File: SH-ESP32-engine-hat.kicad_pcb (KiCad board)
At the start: 2 copper layers, 34 x 58 mm, 66 parts, among them J301 I2C_top, J302 I2C_bottom, J303 GPIO subset, J304 Opto_bottom, J305 1-Wire_top, J306 1-Wire_bottom, J307 Opto_top, J401 Conn_01x02, J402 Conn_01x02, J501 Conn_01x02, J601 Alarm input, Q401 S9015, Q402 S9015, U401 LMV324, U402 RCLAMP0524P-N, U403 RCLAMP0524P-N, U601 ELQ3H7

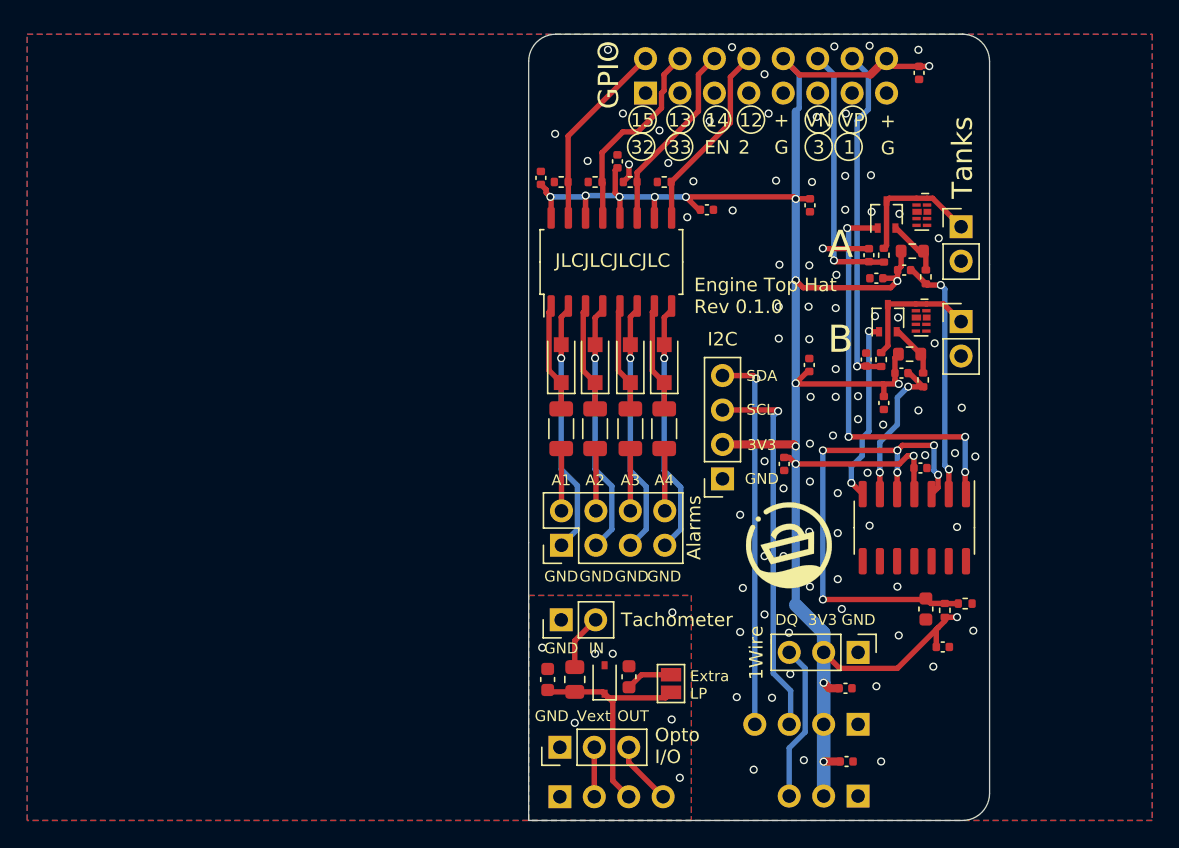
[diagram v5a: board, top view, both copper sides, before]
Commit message: Redesign with unisolated inputs
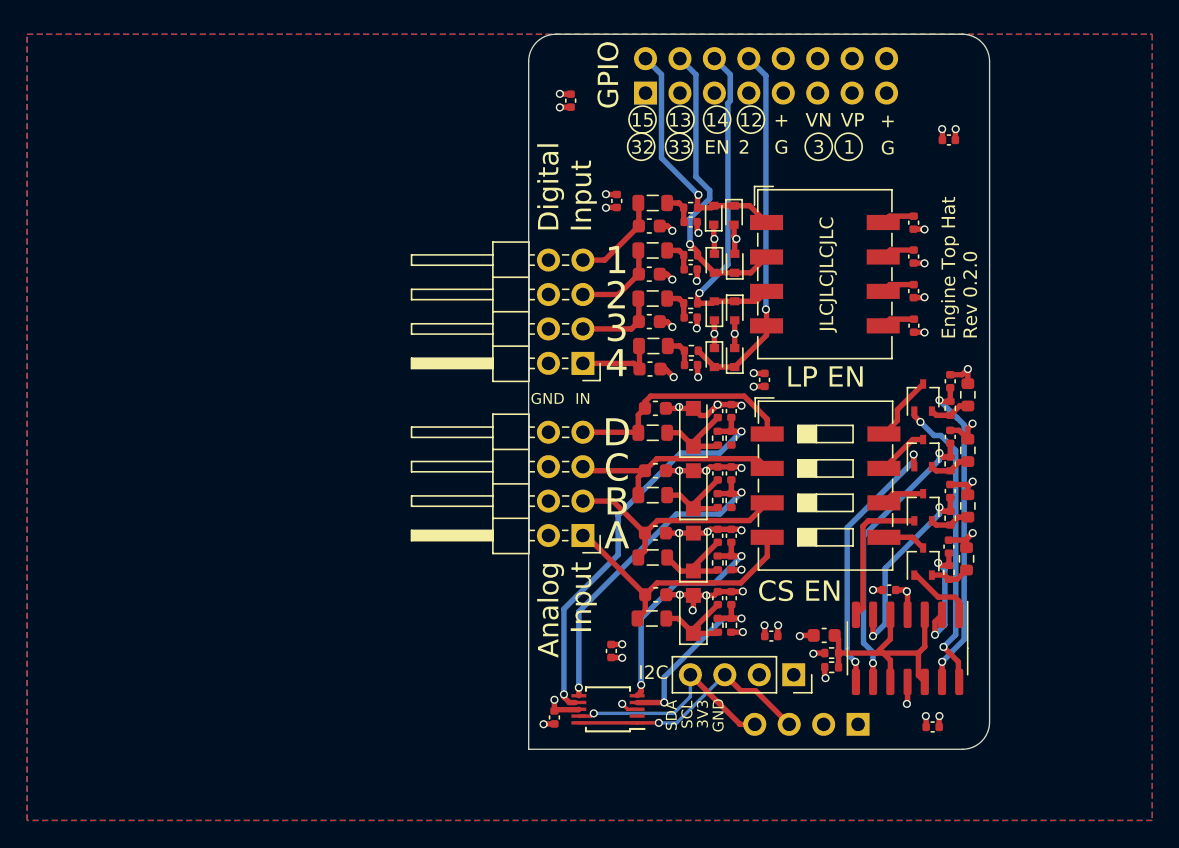
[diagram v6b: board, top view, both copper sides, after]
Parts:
- removed C201, C203, C204, C206, C212: 100nF, Capacitor_SMD:C_0402_1005Metric
- removed C406: 1uF, Capacitor_SMD:C_0402_1005Metric
- removed the C501 at (133.4, 104.4)
- removed the C502 at (127.4, 104.6)
- removed D601, D602, D603, D604: SM4007PL, Diode_SMD:D_SOD-123F
- removed the G*** at (145.2, 94.7)
- removed H202: MountingHole, SH-ESP32:MountingSlot_3.2mm_M3_Unplated
- removed J304: Opto_bottom, Connector_PinSocket_2.54mm:PinSocket_1x04_P2.54mm_Vertical
- removed J305: 1-Wire_top, Connector_PinHeader_2.54mm:PinHeader_1x03_P2.54mm_Vertical
- removed J306: 1-Wire_bottom, Connector_PinSocket_2.54mm:PinSocket_1x03_P2.54mm_Vertical
- removed J307: Opto_top, Connector_PinHeader_2.54mm:PinHeader_1x03_P2.54mm_Vertical
- removed the J402 at (157.9, 78.2)
- removed the J501 at (128.4, 100.2)
- removed J601: Alarm input, Connector_PinHeader_2.54mm:PinHeader_2x04_P2.54mm_Vertical
- removed JP501: SolderJumper_2_Open, Jumper:SolderJumper-2_P1.3mm_Open_Pad1.0x1.5mm
- removed R408: 1.5k, Resistor_SMD:R_0402_1005Metric
- removed the R501 at (129.4, 104.6)
- removed R601, R602, R603, R604: 3.3k, Resistor_SMD:R_1206_3216Metric
- removed R605, R606, R607, R608: 2.2k, Resistor_SMD:R_0402_1005Metric
- removed U402, U403: RCLAMP0524P-N, Package_DFN_QFN:Diodes_UDFN-10_1.0x2.5mm_P0.5mm
- removed U601: ELQ3H7, Package_SO:SOIC-16_4.55x10.3mm_P1.27mm
- added C301: 33pF/50V, Capacitor_SMD:C_0603_1608Metric, F.Cu at (134.9, 71.2)
- added C302: 33pF/50V, Capacitor_SMD:C_0603_1608Metric, F.Cu at (134.9, 74.7)
- added C303: 33pF/50V, Capacitor_SMD:C_0603_1608Metric, F.Cu at (134.9, 78.2)
- added C304: 33pF/50V, Capacitor_SMD:C_0603_1608Metric, F.Cu at (134.9, 81.7)
- added C305: 33pF, Capacitor_SMD:C_0402_1005Metric, F.Cu at (137.9, 70.8)
- added C306: 33pF, Capacitor_SMD:C_0402_1005Metric, F.Cu at (137.9, 74.3)
- added C307: 33pF, Capacitor_SMD:C_0402_1005Metric, F.Cu at (137.9, 77.9)
- added C308: 33pF, Capacitor_SMD:C_0402_1005Metric, F.Cu at (138.0, 81.4)
- added C309: 1.5nF, Capacitor_SMD:C_0402_1005Metric, F.Cu at (154.4, 78.5)
- added C310: 1.5nF, Capacitor_SMD:C_0402_1005Metric, F.Cu at (154.4, 76.0)
- added C311: 1.5nF, Capacitor_SMD:C_0402_1005Metric, F.Cu at (154.4, 73.4)
- added C312: 1.5nF, Capacitor_SMD:C_0402_1005Metric, F.Cu at (154.4, 70.9)
- added C503: 100nF, Capacitor_SMD:C_0402_1005Metric, F.Cu at (157.1, 86.7)
- added C504: 100nF, Capacitor_SMD:C_0402_1005Metric, F.Cu at (157.1, 82.6)
- added C507: 1uF, Capacitor_SMD:C_0603_1608Metric, F.Cu at (135.4, 98.3)
- added C508: 1uF, Capacitor_SMD:C_0603_1608Metric, F.Cu at (135.3, 93.8)
- added C509: 1uF, Capacitor_SMD:C_0603_1608Metric, F.Cu at (135.3, 89.2)
- added C510: 1uF, Capacitor_SMD:C_0603_1608Metric, F.Cu at (135.3, 84.6)
- added C511: 1uF, Capacitor_SMD:C_0402_1005Metric, F.Cu at (139.9, 98.6)
- added C512: 1uF, Capacitor_SMD:C_0402_1005Metric, F.Cu at (139.9, 94.0)
- added C513: 1uF, Capacitor_SMD:C_0402_1005Metric, F.Cu at (139.9, 89.4)
- added C514: 1uF, Capacitor_SMD:C_0402_1005Metric, F.Cu at (139.9, 84.8)
- added C516: 100nF, Capacitor_SMD:C_0402_1005Metric, F.Cu at (140.9, 94.0)
- added C517: 100nF, Capacitor_SMD:C_0402_1005Metric, F.Cu at (140.9, 89.4)
- added C518: 100nF, Capacitor_SMD:C_0402_1005Metric, F.Cu at (140.9, 84.8)
- added C519: 100nF, Capacitor_SMD:C_0402_1005Metric, F.Cu at (127.9, 107.4)
- added D301: MSK4005, Diode_SMD:D_SOD-523, F.Cu at (139.7, 70.3)
- added D302: MSK4005, Diode_SMD:D_SOD-523, F.Cu at (141.2, 70.3)
- added D303: MSK4005, Diode_SMD:D_SOD-523, F.Cu at (139.7, 73.9)
- added D304: MSK4005, Diode_SMD:D_SOD-523, F.Cu at (141.2, 73.9)
- added D305: MSK4005, Diode_SMD:D_SOD-523, F.Cu at (139.7, 77.4)
- added D306: MSK4005, Diode_SMD:D_SOD-523, F.Cu at (141.2, 77.4)
- added D307: MSK4005, Diode_SMD:D_SOD-523, F.Cu at (139.7, 80.8)
- added D308: MSK4005, Diode_SMD:D_SOD-523, F.Cu at (141.2, 80.8)
- added D502: SMF33A, Diode_SMD:D_SOD-123F, F.Cu at (138.2, 95.2)
- added D503: SMF33A, Diode_SMD:D_SOD-123F, F.Cu at (138.2, 90.6)
- added D504: SMF33A, Diode_SMD:D_SOD-123F, F.Cu at (138.2, 86.0)
- added FB301: GZ2012D101TF, Inductor_SMD:L_0805_2012Metric, F.Cu at (135.2, 69.5)
- added FB302: GZ2012D101TF, Inductor_SMD:L_0805_2012Metric, F.Cu at (135.2, 73.0)
- added FB303: GZ2012D101TF, Inductor_SMD:L_0805_2012Metric, F.Cu at (135.2, 76.5)
- added FB304: GZ2012D101TF, Inductor_SMD:L_0805_2012Metric, F.Cu at (135.2, 80.0)
- added FB501: GZ2012D601TF, Inductor_SMD:L_0805_2012Metric, F.Cu at (135.1, 100.1)
- added FB502: GZ2012D601TF, Inductor_SMD:L_0805_2012Metric, F.Cu at (135.2, 95.6)
- added FB503: GZ2012D601TF, Inductor_SMD:L_0805_2012Metric, F.Cu at (135.2, 91.0)
- added FB504: GZ2012D601TF, Inductor_SMD:L_0805_2012Metric, F.Cu at (135.2, 86.4)
- added J301: Conn_02x04_Odd_Even, Connector_PinHeader_2.54mm:PinHeader_2x04_P2.54mm_Horizontal, F.Cu at (130.0, 81.3)
- added Q503: S9015, Package_TO_SOT_SMD:SOT-323_SC-70, F.Cu at (155.1, 87.9)
- added Q504: S9015, Package_TO_SOT_SMD:SOT-323_SC-70, F.Cu at (155.1, 83.8)
- added R301: 47k, Resistor_SMD:R_0402_1005Metric, F.Cu at (137.9, 69.8)
- added R302: 47k, Resistor_SMD:R_0402_1005Metric, F.Cu at (137.9, 73.3)
- added R303: 47k, Resistor_SMD:R_0402_1005Metric, F.Cu at (137.9, 76.8)
- added R304: 47k, Resistor_SMD:R_0402_1005Metric, F.Cu at (138.0, 80.3)
- added R503: 1k, Resistor_SMD:R_0402_1005Metric, F.Cu at (157.1, 88.7)
- added R504: 1k, Resistor_SMD:R_0402_1005Metric, F.Cu at (157.1, 84.6)
- added R507: 30, Resistor_SMD:R_0603_1608Metric, F.Cu at (158.4, 87.7)
- added R508: 30, Resistor_SMD:R_0603_1608Metric, F.Cu at (158.4, 83.6)
- added R512: 1k, Resistor_SMD:R_0402_1005Metric, F.Cu at (140.9, 100.6)
- added R513: 13k, Resistor_SMD:R_0402_1005Metric, F.Cu at (139.9, 96.0)
- added R514: 1k, Resistor_SMD:R_0402_1005Metric, F.Cu at (140.9, 96.0)
- added R515: 13k, Resistor_SMD:R_0402_1005Metric, F.Cu at (139.9, 91.4)
- added R516: 1k, Resistor_SMD:R_0402_1005Metric, F.Cu at (140.9, 91.4)
- added R517: 13k, Resistor_SMD:R_0402_1005Metric, F.Cu at (139.9, 86.8)
- added R518: 1k, Resistor_SMD:R_0402_1005Metric, F.Cu at (140.9, 86.8)
- added SW301: SW_DIP_x04, Button_Switch_SMD:SW_DIP_SPSTx04_Slide_9.78x12.34mm_W8.61mm_P2.54mm, F.Cu at (147.8, 74.7)
- added SW501: SW_DIP_x04, Button_Switch_SMD:SW_DIP_SPSTx04_Slide_9.78x12.34mm_W8.61mm_P2.54mm, F.Cu at (147.9, 90.3)
- added U502: ADS1115IDGS, Package_SO:TSSOP-10_3x3mm_P0.5mm, F.Cu at (131.8, 106.8)
- C515: renamed from C405; value 1uF -> 100nF
- D501: value BZT52C16S -> SMF33A; footprint Diode_SMD:D_SOD-323 -> Diode_SMD:D_SOD-123F
- J501: renamed from J401; value Conn_01x02 -> Conn_02x04; footprint Connector_PinHeader_2.54mm:PinHeader_1x02_P2.54mm_Vertical -> Connector_PinHeader_2.54mm:PinHeader_2x04_P2.54mm_Horizontal
- R511: renamed from R407; value 1.5k -> 13k
- moved J501 36.0 mm to (130.0, 94.0), turned to 180 degrees
- moved C207 32.1 mm to (129.1, 61.9)
- moved R511 29.9 mm to (139.9, 100.6), turned to 270 degrees
- moved C515 27.3 mm to (140.9, 98.6)
- moved Q501 25.7 mm to (155.1, 95.9)
- moved R505 23.0 mm to (158.3, 95.7), turned to 270 degrees
- moved R501 21.9 mm to (157.0, 96.7), turned to 90 degrees
- moved C501 20.7 mm to (157.0, 94.8), turned to 90 degrees
- moved C210 18.6 mm to (157.0, 64.8)
- moved C209 17.5 mm to (132.1, 102.5), turned to 270 degrees
- moved J401 15.4 mm to (145.6, 104.2), turned to 270 degrees
- moved Q502 14.2 mm to (155.1, 91.9)
- moved C208 13.3 mm to (143.4, 82.5), turned to 270 degrees
- moved C205 12.7 mm to (143.9, 101.4)
- moved R506 12.0 mm to (158.4, 91.8), turned to 270 degrees
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- renumbered C401 to C501, C402 to C502, C403 to C505, C404 to C506, J301 to J401, J302 to J402, J303 to J403, Q401 to Q501, Q402 to Q502, R401 to R501, R402 to R502, R403 to R505, R404 to R506, R405 to R509, R406 to R510, U401 to U501
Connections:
- net /IOHeader/SCL renamed /Analog input/SCL
- net /IOHeader/SDA renamed /Analog input/SDA
- C506 pad 1: /Tank sender/Vin -> /Analog input/Vin
- C515 pad 1: /Tank sender/ADC_A -> /Analog input/ADC_A
- D501 pad 1: /ISO_IN -> /Analog input/InFA
- D501 pad 2: ISO_GND -> GND
- J403 pad 12: /Tank sender/ADC_A -> (no net)
- J403 pad 14: /Tank sender/ADC_B -> (no net)
- J403 pad 2: /AL1 -> /DI1
- J403 pad 4: /AL2 -> /DI2
- J403 pad 6: /AL3 -> /DI3
- J403 pad 8: /AL4 -> /DI4
- J501 pad 1: /Tank sender/VoutA -> /Analog input/InA
- Q501 pad 3: /Tank sender/VoutA -> /Analog input/IoutA
- Q502 pad 3: /Tank sender/VoutB -> /Analog input/IoutB
- R509 pad 2: /Tank sender/Vin -> /Analog input/Vin
- R510 pad 1: /Tank sender/Vin -> /Analog input/Vin
- R511 pad 1: /Tank sender/ADC_A -> /Analog input/ADC_A
- R511 pad 2: /Tank sender/VoutA -> /Analog input/InFA
- U501 pad 10: GND -> /Analog input/Vin
- U501 pad 12: GND -> /Analog input/Vin
- U501 pad 13: GND -> Net-(C504-Pad1)
- U501 pad 14: (no net) -> Net-(Q504-Pad1)
- U501 pad 3: /Tank sender/Vin -> /Analog input/Vin
- U501 pad 5: /Tank sender/Vin -> /Analog input/Vin
- U501 pad 8: (no net) -> Net-(Q503-Pad1)
- U501 pad 9: GND -> Net-(C503-Pad1)
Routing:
- net +3V3: track 155.4 -> 27.5 mm, vias 17 -> 16
- net GND: track 4.88 -> 53.6 mm, vias 82 -> 42
- net /Tank sender/Vin: track 36.7 -> 0.00 mm, vias 6 -> 0
- net /Analog input/ADC_D: track 0.00 -> 30.5 mm, vias 0 -> 2
- net /DI4: track 0.00 -> 27.5 mm, vias 0 -> 1
- net Net-(Q501-Pad1): track 30.5 -> 5.09 mm, vias 4 -> 0
- net /Tank sender/ADC_B: track 25.3 -> 0.00 mm, vias 1 -> 0
- net /DI3: track 0.00 -> 25.0 mm, vias 0 -> 1
- net /Analog input/ADC_C: track 0.00 -> 24.6 mm, vias 0 -> 2
- net Net-(C504-Pad1): track 0.00 -> 24.1 mm, vias 0 -> 2
- net /DI2: track 0.00 -> 22.4 mm, vias 0 -> 1
- net Net-(Q504-Pad1): track 0.00 -> 22.4 mm, vias 0 -> 2
- net Net-(C503-Pad1): track 0.00 -> 21.4 mm, vias 0 -> 2
- net Net-(Q503-Pad1): track 0.00 -> 20.0 mm, vias 0 -> 2
- net /Analog input/InA: track 0.00 -> 20.0 mm
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- added copper zone on In2.Cu, net +3V3
- added copper zone on In1.Cu, net GND
- removed copper zone on B.Cu, net ISO_GND
- removed copper zone on F.Cu, net ISO_GND
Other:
- board size 34 x 58 mm -> 34 x 52.8 mm
- copper layers 2 -> 4
- board text added: "4"
- board text added: "Analog Input"
- board text added: "C"
- board text added: "CS EN"
- board text added: "D"
- board text added: "Digital Input"
- board text added: "Engine Top Hat Rev 0.2.0"
- board text added: "LP EN"
- board text removed: "1Wire"
- board text removed: "A1"
- board text removed: "A2"
- board text removed: "A3"
- board text removed: "A4"
- board text removed: "Alarms"
- board text removed: "DQ"
- board text removed: "Engine Top Hat Rev 0.1.0"
- board text removed: "Extra LP"
- board text removed: "OUT"
- board text removed: "Opto I/O"
- board text removed: "Tachometer"
- board text removed: "Tanks"
- board text removed: "Vext"

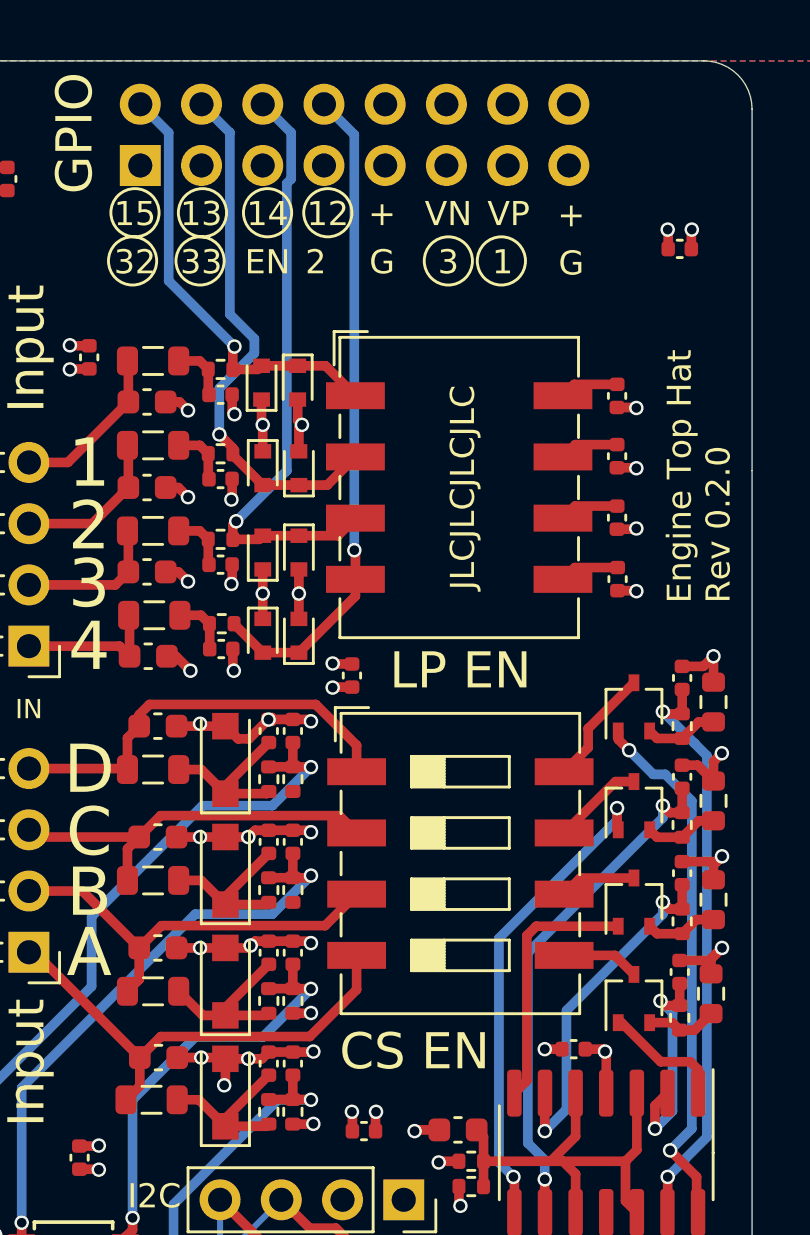
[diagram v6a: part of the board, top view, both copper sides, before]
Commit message: Change DIP switches to headers
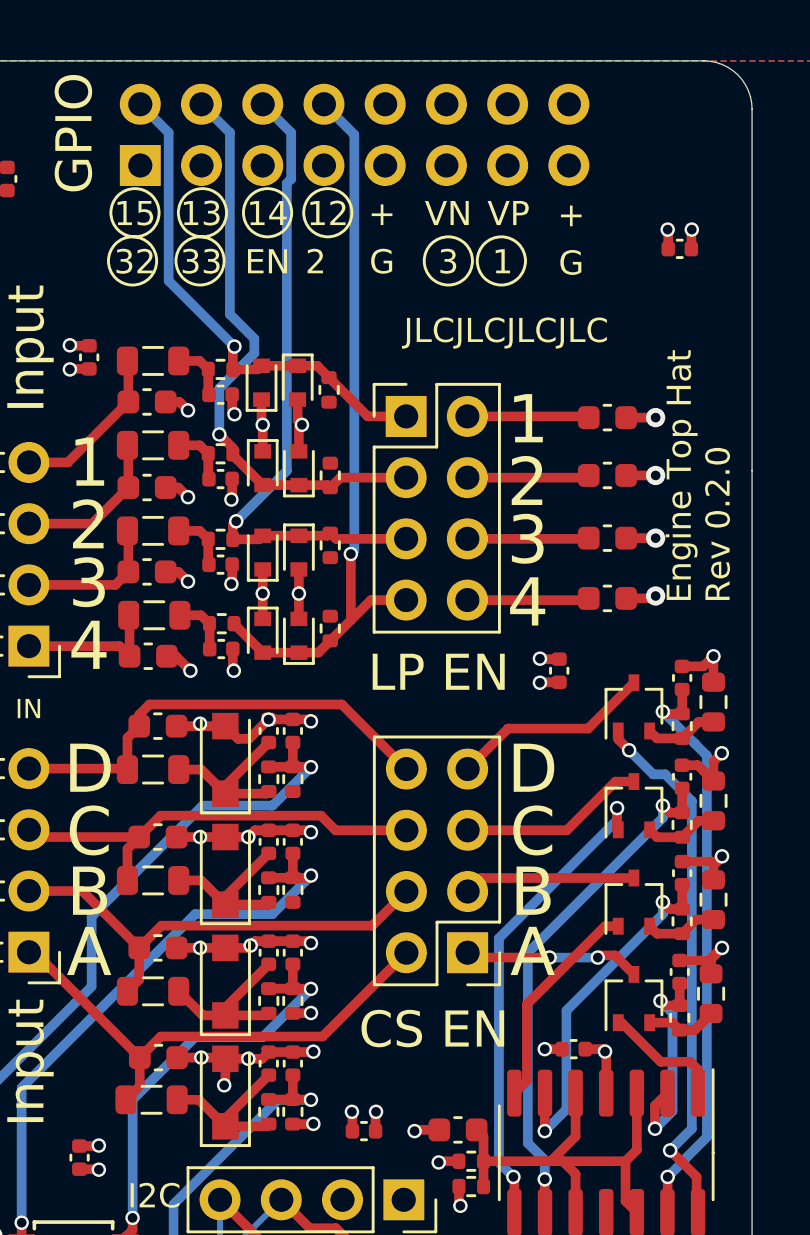
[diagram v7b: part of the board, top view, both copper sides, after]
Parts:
- removed SW301, SW501: SW_DIP_x04, Button_Switch_SMD:SW_DIP_SPSTx04_Slide_9.78x12.34mm_W8.61mm_P2.54mm
- added J302: Conn_02x04_Odd_Even, Connector_PinHeader_2.54mm:PinHeader_2x04_P2.54mm_Vertical, F.Cu at (145.7, 71.8)
- added J501: Conn_02x04_Odd_Even, Connector_PinHeader_2.54mm:PinHeader_2x04_P2.54mm_Vertical, F.Cu at (148.2, 94.0)
- added R305: 1M, Resistor_SMD:R_0402_1005Metric, F.Cu at (142.4, 70.7)
- added R306: 1M, Resistor_SMD:R_0402_1005Metric, F.Cu at (142.5, 74.2)
- added R307: 1M, Resistor_SMD:R_0402_1005Metric, F.Cu at (142.5, 77.1)
- added R308: 1M, Resistor_SMD:R_0402_1005Metric, F.Cu at (142.5, 80.5)
- C309, C310, C311, C312: value 1.5nF -> 680pF; footprint Capacitor_SMD:C_0402_1005Metric -> Capacitor_SMD:C_0603_1608Metric
- C515, C516, C517, C518: value 100nF -> 470nF
- R301, R302, R303, R304: value 47k -> 100k
- R511, R513, R515, R517: value 13k -> 51k
- R512, R514, R516, R518: value 1k -> 3.9k
- moved G*** 10.0 mm to (139.2, 98.1)
- moved REF** 10.0 mm to (139.2, 92.1)
- moved C204 8.60 mm to (152.0, 82.3)
- moved G*** 7.09 mm to (154.2, 96.2), turned to 90 degrees
- moved C312 0.98 mm to (154.0, 71.8), turned to 0 degrees
- moved C310 0.94 mm to (154.0, 76.8), turned to 0 degrees
- moved C309 0.90 mm to (154.0, 79.3), turned to 0 degrees
- moved C311 0.89 mm to (154.0, 74.2), turned to 0 degrees
- renumbered C202 to C201, C205 to C202, C207 to C203, C208 to C204, C209 to C205, C210 to C206, C211 to C207, J501 to J502
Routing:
- net /Analog input/IoutA: track 3.22 -> 7.35 mm, vias 0 -> 2
- net /Analog input/IoutC: track 3.78 -> 7.74 mm
- net /Analog input/IoutB: track 3.17 -> 7.13 mm
- net /Analog input/IoutD: track 4.89 -> 8.38 mm
- net /DI4: track 27.5 -> 30.5 mm
- net Net-(C312-Pad1): track 2.44 -> 5.06 mm
- net Net-(C311-Pad1): track 2.46 -> 5.07 mm
- net Net-(C309-Pad1): track 2.47 -> 5.06 mm
- net Net-(C310-Pad1): track 2.45 -> 5.05 mm
- net /DI1: track 18.3 -> 20.8 mm
- net /Analog input/InB: track 17.5 -> 19.6 mm
- net /Analog input/InC: track 16.4 -> 18.4 mm
- net /DI3: track 25.0 -> 26.9 mm
- net /DI2: track 22.4 -> 24.2 mm
- net GND: track 53.6 -> 55.4 mm
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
